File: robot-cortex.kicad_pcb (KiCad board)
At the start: 2 copper layers, 36 parts, among them IC1 ADP2301AUJZ-R7, J1 USB4110GFA, Q1 SS8050-G, Q2 SS8050-G, U1 DF52-4S-0.8H(21), U2 ESP32-WROOM-32E-H4, U3 DF52-5S-0.8H(21), U5 CP2102N-A02-GQFN24R

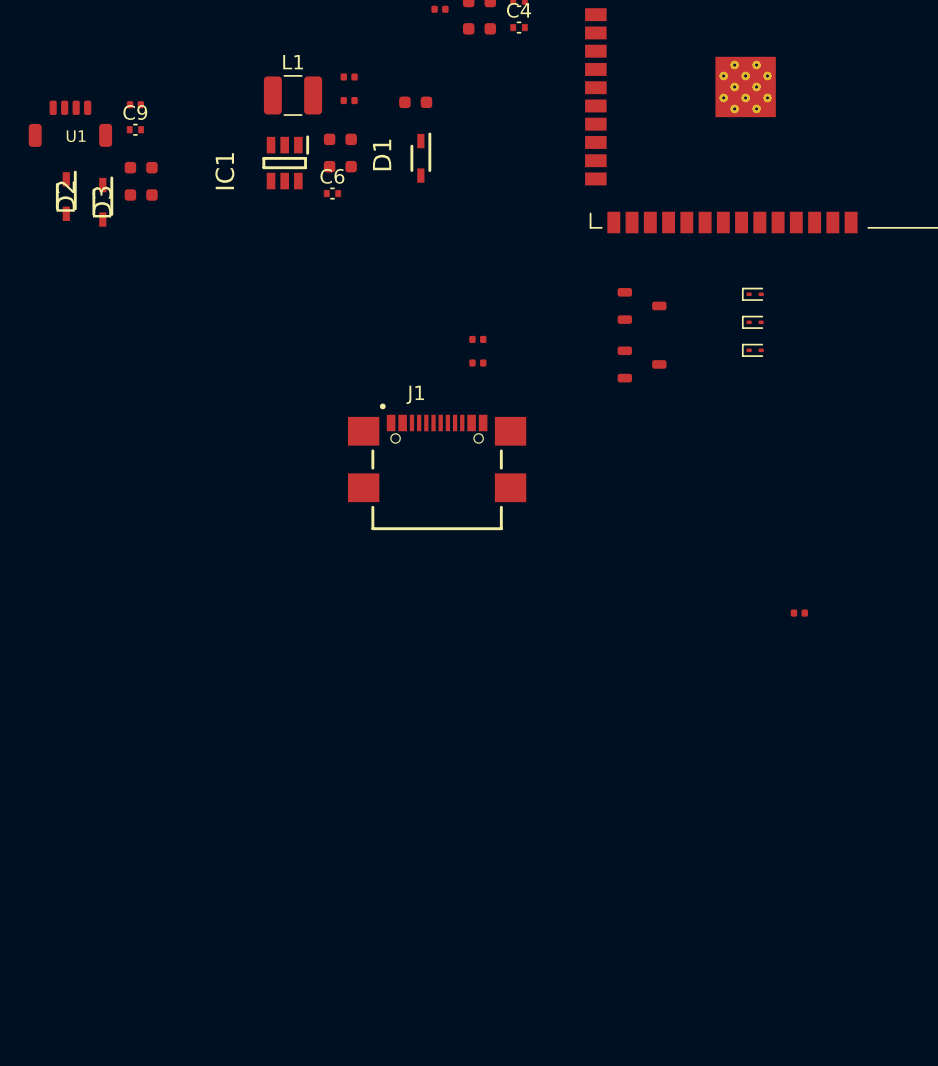
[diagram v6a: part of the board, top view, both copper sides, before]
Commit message: nearly ready to route, need to decide on 5V issue for CAN still
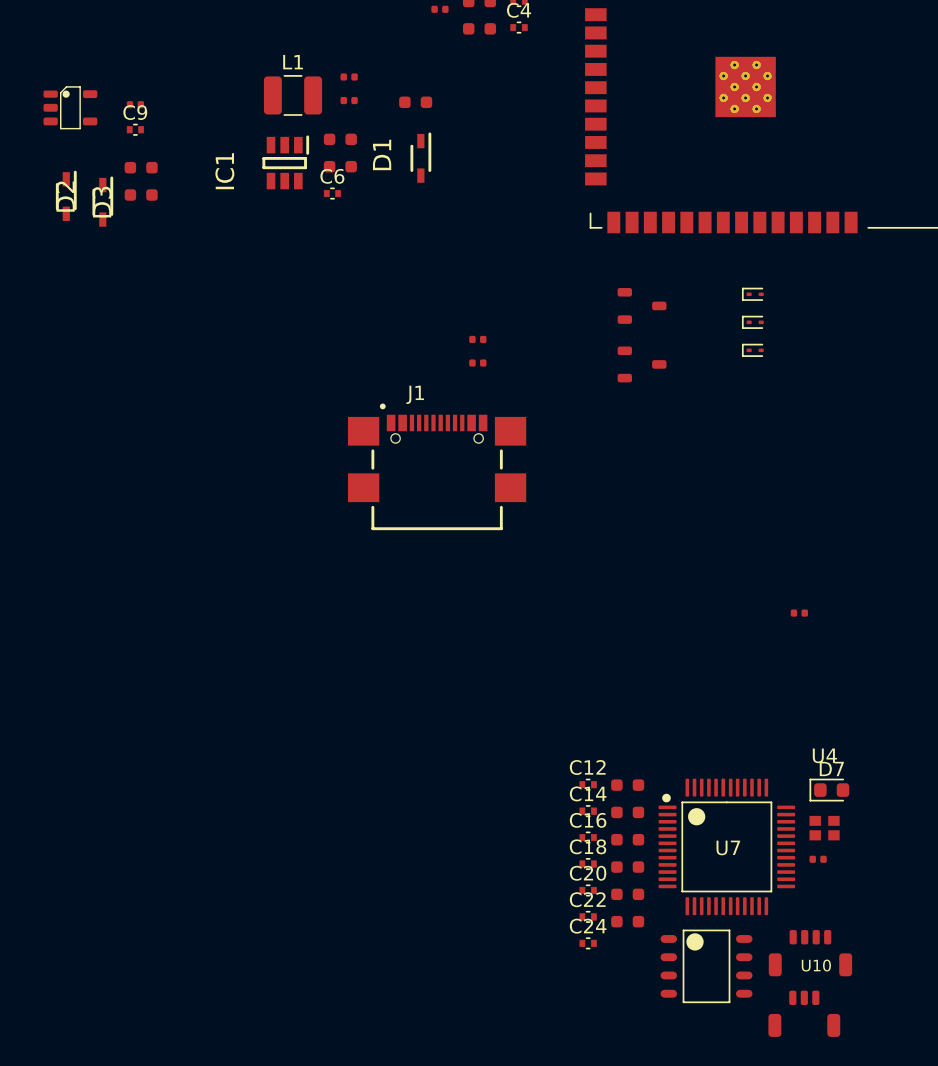
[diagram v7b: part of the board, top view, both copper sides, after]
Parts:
- added C12: 100nF, robot-cortex:C_0402_1005Metric, F.Cu at (85.6, 101.1)
- added C13: C2998534, robot-cortex:C_0603_1608Metric, F.Cu at (88.4, 101.1)
- added C14: 100nF, robot-cortex:C_0402_1005Metric, F.Cu at (85.6, 102.9)
- added C15: C2998534, robot-cortex:C_0603_1608Metric, F.Cu at (88.4, 103.0)
- added C16: 100nF, robot-cortex:C_0402_1005Metric, F.Cu at (85.6, 104.8)
- added C17: C2998534, robot-cortex:C_0603_1608Metric, F.Cu at (88.4, 104.9)
- added C18: 100nF, robot-cortex:C_0402_1005Metric, F.Cu at (85.6, 106.6)
- added C19: C2998534, robot-cortex:C_0603_1608Metric, F.Cu at (88.4, 106.8)
- added C20: 100nF, robot-cortex:C_0402_1005Metric, F.Cu at (85.6, 108.5)
- added C21: C2998534, robot-cortex:C_0603_1608Metric, F.Cu at (88.4, 108.7)
- added C22: 100nF, robot-cortex:C_0402_1005Metric, F.Cu at (85.6, 110.3)
- added C23: C2998534, robot-cortex:C_0603_1608Metric, F.Cu at (88.4, 110.6)
- added C24: 100nF, robot-cortex:C_0402_1005Metric, F.Cu at (85.6, 112.1)
- added D7: C84264, robot-cortex:LED_0603_1608Metric, F.Cu at (102.6, 101.5)
- added R10: 470, robot-cortex:R_0402_1005Metric, F.Cu at (101.6, 106.3)
- added U10: DF52-4S-0.8H(21), robot-cortex:DF52-4S-0.8H(21), F.Cu at (101.1, 111.7)
- added U4: C2901617, robot-cortex:ECS-1633-480-BN-TR, F.Cu at (102.1, 104.1)
- added U7: STM32G431CBT6, robot-cortex:LQFP48-STM32, F.Cu at (95.3, 105.4)
- added U8: TLE9250XSJXUMA1, robot-cortex:SOIC8-TLE5009, F.Cu at (93.9, 113.7)
- added U9: DF52-3S-0.8H(21), robot-cortex:DF52-3S-0.8H(21), F.Cu at (100.7, 115.9)
- U1: value DF52-4S-0.8H(21) -> SPX3819M5-L-5-0; footprint robot-cortex:DF52-4S-0.8H(21) -> robot-cortex:SOT-23-5
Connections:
- net /3V3-Supply/VIN renamed /VDD_MIXED
- net 3v3 renamed +3V3
- U1 pad 2: /VBAT -> GND
- U1 pad 3: GND -> /VBAT
- U1 pad 4: GND -> unconnected-(U1-BYP-Pad4)
- U1 pad 5: GND -> /+5V0
- U2 pad 12: unconnected-(U2-IO27-Pad12) -> /BOOT
- U2 pad 24: unconnected-(U2-IO2-Pad24) -> /NRST
- U2 pad 27: /ESP32/ESP_UART2_RX -> /UART2_TX
- U2 pad 28: /ESP32/ESP_UART2_TX -> /UART2_RX
- U2 pad 29: /ESP32/ESP32_SS -> /SS
- U2 pad 30: /ESP32/ESP32_SCK -> /SPI1_SCK
- U2 pad 31: /ESP32/ESP32_MISO -> /SPI1_MISO
- U2 pad 37: /ESP32/ESP32_MOSI -> /SPI1_MOSI

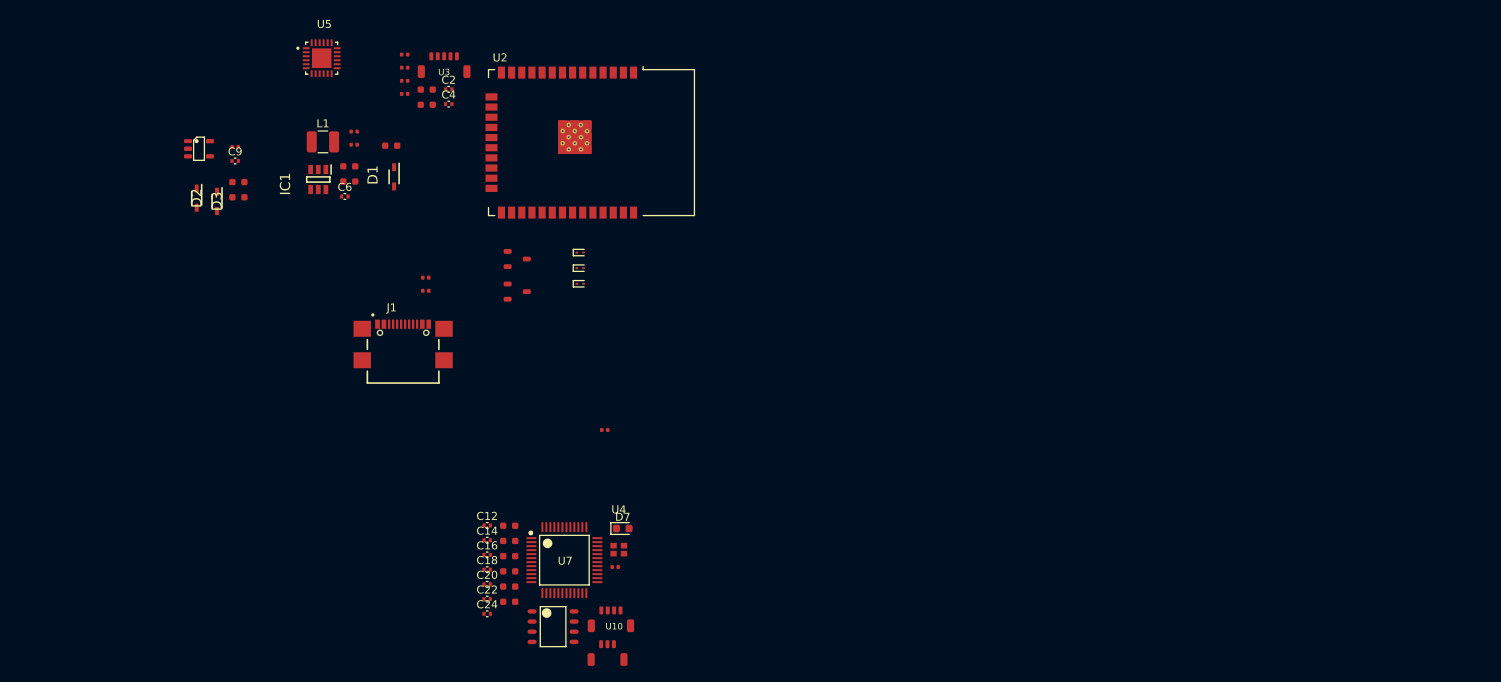
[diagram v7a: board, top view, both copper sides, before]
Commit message: updated power supply method
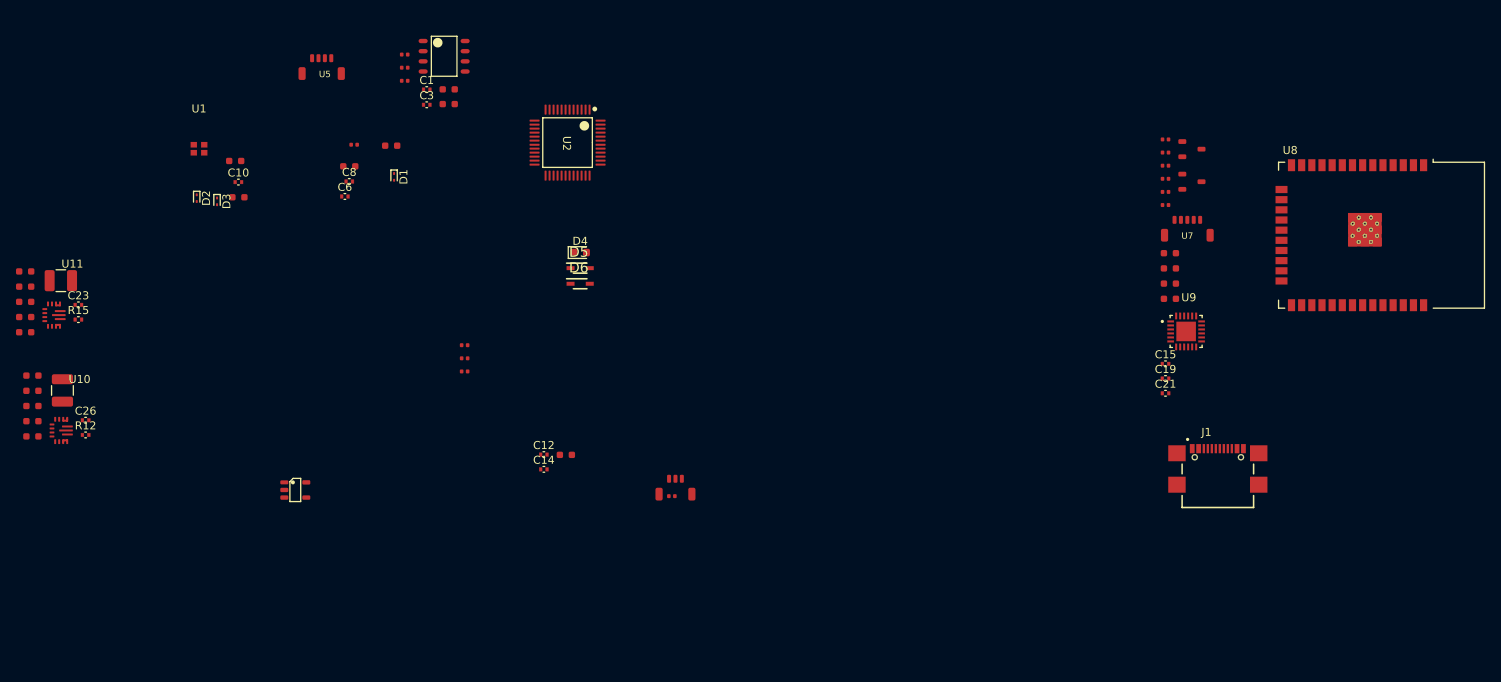
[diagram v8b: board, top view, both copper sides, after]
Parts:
- removed D7: C84264, robot-cortex:LED_0603_1608Metric
- removed IC1: ADP2301AUJZ-R7, robot-cortex:SOT95P280X100-6N
- added C25: C386081, robot-cortex:C_0603_1608Metric, F.Cu at (28.8, 82.3)
- added C26: 100nF, robot-cortex:C_0402_1005Metric, F.Cu at (35.4, 87.9)
- added C27: C2998534, robot-cortex:C_0603_1608Metric, F.Cu at (28.8, 84.2)
- added C28: C2998534, robot-cortex:C_0603_1608Metric, F.Cu at (28.8, 86.2)
- added C29: C2998534, robot-cortex:C_0603_1608Metric, F.Cu at (28.8, 88.0)
- added C30: C2998534, robot-cortex:C_0603_1608Metric, F.Cu at (28.8, 90.0)
- added C31: C2998534, robot-cortex:C_0603_1608Metric, F.Cu at (27.9, 73.1)
- added C32: C2998534, robot-cortex:C_0603_1608Metric, F.Cu at (27.9, 75.0)
- added C33: C2998534, robot-cortex:C_0603_1608Metric, F.Cu at (27.9, 76.9)
- added L2: 1277AS-H-1R0M=P2, robot-cortex:L_1210_3225Metric, F.Cu at (32.5, 84.2)
- added R12: 100k, robot-cortex:C_0402_1005Metric, F.Cu at (35.4, 89.8)
- added R13: 680k, robot-cortex:R_0402_1005Metric, F.Cu at (82.8, 78.5)
- added R14: 130k, robot-cortex:R_0402_1005Metric, F.Cu at (82.8, 80.2)
- added R15: 100k, robot-cortex:C_0402_1005Metric, F.Cu at (34.5, 75.3)
- added R16: 0, robot-cortex:R_0402_1005Metric, F.Cu at (82.8, 81.8)
- added U11: TPS63070, robot-cortex:VQFN-TPS63070, F.Cu at (31.5, 74.8)
- added U6: SPX3819M5-L-5-0, robot-cortex:SOT-23-5, F.Cu at (61.6, 96.6)
- C1, C10, C3, C8: value 4.7uF -> 100nF; footprint robot-cortex:C_0603_1608Metric -> robot-cortex:C_0402_1005Metric
- C11, C5, C7: value 4.7uF -> C2998534
- C15, C19, C21, C23: value C2998534 -> 100nF; footprint robot-cortex:C_0603_1608Metric -> robot-cortex:C_0402_1005Metric
- C16, C18, C20, C4: value 100nF -> 4.7uF; footprint robot-cortex:C_0402_1005Metric -> robot-cortex:C_0603_1608Metric
- C17: value C2998534 -> 4.7uF
- C2, C24, C9: value 100nF -> C2998534; footprint robot-cortex:C_0402_1005Metric -> robot-cortex:C_0603_1608Metric
- C22: value 100nF -> C386081; footprint robot-cortex:C_0402_1005Metric -> robot-cortex:C_0603_1608Metric
- D1, D2, D3: value NSR0530HT1G -> ESD9B3.3ST5G; footprint robot-cortex:SOD2512X110N -> robot-cortex:D_SOD-923
- D4: value ESD9B3.3ST5G -> C84264; footprint robot-cortex:D_SOD-923 -> robot-cortex:LED_0603_1608Metric
- D5, D6: value ESD9B3.3ST5G -> NSR0530HT1G; footprint robot-cortex:D_SOD-923 -> robot-cortex:SOD2512X110N
- L1: value 2.2uH -> 1277AS-H-1R0M=P2; footprint Inductor_SMD:L_1210_3225Metric -> robot-cortex:L_1210_3225Metric
- R1, R2: value 10k -> 5.1k
- R10: value 470 -> 470k
- R11: value 10.2k -> 150k
- R3: value 1k -> 470
- R4: value 22k -> 10k
- R5: value 31.6k -> 10k
- R7: value 5.1k -> 22k
- R8: value 5.1k -> 47.5k
- R9: value 47.5k -> 1k
- U1: value SPX3819M5-L-5-0 -> C2901617; footprint robot-cortex:SOT-23-5 -> robot-cortex:ECS-1633-480-BN-TR
- U10: value DF52-4S-0.8H(21) -> TPS63070; footprint robot-cortex:DF52-4S-0.8H(21) -> robot-cortex:VQFN-TPS63070
- U2: value ESP32-WROOM-32E-H4 -> STM32G431CBT6; footprint robot-cortex:ESP32-WROOM-32 -> robot-cortex:LQFP48-STM32
- U3: value DF52-5S-0.8H(21) -> TLE9250XSJXUMA1; footprint robot-cortex:DF52-5S-0.8H(21) -> robot-cortex:SOIC8-TLE5009
- U4: value C2901617 -> DF52-3S-0.8H(21); footprint robot-cortex:ECS-1633-480-BN-TR -> robot-cortex:DF52-3S-0.8H(21)
- U5: value CP2102N-A02-GQFN24R -> DF52-4S-0.8H(21); footprint robot-cortex:QFN50P400X400X80-25N -> robot-cortex:DF52-4S-0.8H(21)
- U7: value STM32G431CBT6 -> DF52-5S-0.8H(21); footprint robot-cortex:LQFP48-STM32 -> robot-cortex:DF52-5S-0.8H(21)
- U8: value TLE9250XSJXUMA1 -> ESP32-WROOM-32E-H4; footprint robot-cortex:SOIC8-TLE5009 -> robot-cortex:ESP32-WROOM-32
- U9: value DF52-3S-0.8H(21) -> CP2102N-A02-GQFN24R; footprint robot-cortex:DF52-3S-0.8H(21) -> robot-cortex:QFN50P400X400X80-25N
- moved R6 116.3 mm to (170.4, 56.1)
- moved U8 111.8 mm to (194.4, 64.8), turned to -90 degrees
- moved J1 103.0 mm to (176.9, 92.6)
- moved R5 101.5 mm to (170.4, 54.5)
- moved R4 95.3 mm to (170.4, 52.8)
- moved C16 93.3 mm to (171.0, 67.0)
- moved R7 93.3 mm to (170.4, 57.8)
- moved R8 93.3 mm to (170.4, 59.4)
- moved C18 92.5 mm to (171.0, 70.8)
- moved C20 92.5 mm to (171.0, 72.8)
- moved C17 90.1 mm to (171.0, 69.0)
- moved U7 88.7 mm to (173.1, 62.9)
- moved C21 85.5 mm to (170.4, 84.6)
- moved C19 85.5 mm to (170.4, 82.7)
- moved Q1 85.5 mm to (173.7, 54.0)
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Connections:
- C1 pad 1: +3V3 -> /NRST
- C11 pad 1: +3V3 -> /VBAT
- C12 pad 1: /NRST -> /VBAT
- C13 pad 1: +3V3 -> /+5V0
- C14 pad 1: +3V3 -> /+5V0
- C15 pad 1: +3V3 -> /ESP32/EN
- C21 pad 1: /VBAT -> +3V3
- C22 pad 1: /VBAT -> /VDD_MIXED
- C23 pad 1: /+5V0 -> Net-(U11-VAUX)
- C4 pad 1: +3V3 -> /VUSB
- C5 pad 1: /VUSB -> +3V3
- C6 pad 1: Net-(IC1-BST) -> +3V3
- C6 pad 2: Net-(D1-K) -> GND
- C9 pad 1: /ESP32/EN -> +3V3
- D1 pad 1: Net-(D1-K) -> GND
- D1 pad 2: GND -> /D-
- D2 pad 1: /VDD_MIXED -> GND
- D2 pad 2: /VBAT -> /D+
- D3 pad 1: /VDD_MIXED -> GND
- D4 pad 1: GND -> Net-(D4-K)
- D4 pad 2: /VUSB -> /LED
- D5 pad 1: GND -> /VDD_MIXED
- D5 pad 2: /D+ -> /VBAT
- D6 pad 1: GND -> /VDD_MIXED
- D6 pad 2: /D- -> /VUSB
- L1 pad 1: Net-(D1-K) -> Net-(U11-L1)
- L1 pad 2: +3V3 -> Net-(U11-L2)
- R1 pad 1: /ESP32/RTS -> GND
- R1 pad 2: Net-(Q2-B) -> Net-(J1-CC1)
- R10 pad 1: Net-(D7-K) -> +3V3
- R10 pad 2: GND -> /PSU_TPS63070RNMR/FB
- R11 pad 1: GND -> /PSU_TPS63070RNMR/FB
- R11 pad 2: /3V3-Supply/FB -> GND
- R2 pad 1: /ESP32/DTR -> GND
- R2 pad 2: Net-(Q1-B) -> Net-(J1-CC2)
- R3 pad 1: Net-(U5-~{RST}) -> Net-(D4-K)
- R3 pad 2: +3V3 -> GND
- R4 pad 1: /ESP32/CP210x_VBUS -> /ESP32/EN
- R4 pad 2: /VUSB -> +3V3
- R5 pad 1: /3V3-Supply/FB -> /ESP32/RTS
- R5 pad 2: +3V3 -> Net-(Q2-B)
- R6 pad 1: /ESP32/EN -> /ESP32/DTR
- R6 pad 2: +3V3 -> Net-(Q1-B)
- R7 pad 1: GND -> /ESP32/CP210x_VBUS
- R7 pad 2: Net-(J1-CC1) -> /VUSB
- R8 pad 2: Net-(J1-CC2) -> /ESP32/CP210x_VBUS
- R9 pad 1: GND -> Net-(U9-~{RST})
- R9 pad 2: /ESP32/CP210x_VBUS -> +3V3
- U1 pad 1: /VBAT -> +3V3
- U1 pad 3: /VBAT -> Net-(U1-OUTPUT)
- U1 pad 4: unconnected-(U1-BYP-Pad4) -> +3V3
- U10 pad 1: /VBAT -> /VDD_MIXED
- U10 pad 2: /CANL -> Net-(U10-PG)
- U10 pad 3: /CANH -> Net-(U10-VAUX)
- U10 pad 5: GND -> /PSU_TPS63070RNMR/FB
- U2 pad 1: GND -> +3V3
- U2 pad 10: unconnected-(U2-IO25-Pad10) -> /UART2_TX
- U2 pad 11: unconnected-(U2-IO26-Pad11) -> /UART2_RX
- U2 pad 12: /BOOT -> unconnected-(U2-PA4-Pad12)
- U2 pad 13: /ESP32/TMS -> unconnected-(U2-PA5-Pad13)
- U2 pad 14: /ESP32/TDI -> unconnected-(U2-PA6-Pad14)
- U2 pad 15: GND -> unconnected-(U2-PA7-Pad15)
- U2 pad 16: /ESP32/TCK -> /ISENSE_A
- U2 pad 17: unconnected-(U2-NC-Pad17) -> /ISENSE_B
- U2 pad 19: unconnected-(U2-NC-Pad19) -> GND
- U2 pad 2: +3V3 -> unconnected-(U2-PC13-Pad2)
- U2 pad 20: unconnected-(U2-NC-Pad20) -> +3V3
- U2 pad 21: unconnected-(U2-NC-Pad21) -> +3V3
- U2 pad 22: unconnected-(U2-NC-Pad22) -> /LED
- U2 pad 23: /ESP32/TDO -> GND
- U2 pad 24: /NRST -> +3V3
- U2 pad 25: /ESP32/IO0 -> /ISENSE_C
- U2 pad 26: unconnected-(U2-IO4-Pad26) -> /ENABLE
- U2 pad 27: /UART2_TX -> unconnected-(U2-PB13-Pad27)
- U2 pad 28: /UART2_RX -> unconnected-(U2-PB14-Pad28)
- U2 pad 29: /SS -> unconnected-(U2-PB15-Pad29)
- U2 pad 3: /ESP32/EN -> unconnected-(U2-PC14-Pad3)
- U2 pad 30: /SPI1_SCK -> unconnected-(U2-PA8-Pad30)
- U2 pad 31: /SPI1_MISO -> unconnected-(U2-PA9-Pad31)
- U2 pad 33: unconnected-(U2-IO21-Pad33) -> /FDCAN1_RX
- U2 pad 34: /ESP32/CP210x_TX -> /FDCAN1_TX
- U2 pad 35: /ESP32/CP210x_RX -> GND
- U2 pad 36: unconnected-(U2-IO22-Pad36) -> +3V3
- U2 pad 37: /SPI1_MOSI -> /SWDIO
- U2 pad 38: GND -> /SWCLK
- U2 pad 39: GND -> unconnected-(U2-PA15-Pad39)
- U2 pad 5: unconnected-(U2-SENSOR_VN-Pad5) -> Net-(U1-OUTPUT)
- U2 pad 7: unconnected-(U2-IO35-Pad7) -> /NRST
- U2 pad 8: unconnected-(U2-IO32-Pad8) -> /COS
- U2 pad 9: unconnected-(U2-IO33-Pad9) -> /SIN
- U3 pad 1: /ESP32/TDO -> /FDCAN1_TX
- U3 pad 2: /ESP32/TMS -> GND
- U3 pad 3: /ESP32/TDI -> /+5V0
- U3 pad 4: /ESP32/TCK -> /FDCAN1_RX
- U3 pad 5: GND -> +3V3
- U3 pad 6: GND -> /CANL
- U3 pad 7: GND -> /CANH
- U4 pad 1: +3V3 -> /SWDIO
- U4 pad 2: GND -> /SWCLK
- U4 pad 3: Net-(U4-OUTPUT) -> GND
- U4 pad 4: +3V3 -> GND
- U5 pad 1: unconnected-(U5-~{RI}/CLK-Pad1) -> /VBAT
- U5 pad 2: GND -> /CANL
- U5 pad 3: /D+ -> /CANH
- U5 pad 4: /D- -> GND
- U5 pad 5: +3V3 -> GND
- U5 pad 6: +3V3 -> GND
- U7 pad 1: +3V3 -> /ESP32/TDO
- U7 pad 2: unconnected-(U7-PC13-Pad2) -> /ESP32/TMS
- U7 pad 3: unconnected-(U7-PC14-Pad3) -> /ESP32/TDI
- U7 pad 4: unconnected-(U7-PC15-Pad4) -> /ESP32/TCK
- U7 pad 5: Net-(U4-OUTPUT) -> GND
- U7 pad 6: unconnected-(U7-PF1-OSC_OUT-Pad6) -> GND
- U7 pad 7: /NRST -> GND
- U8 pad 1: /FDCAN1_TX -> GND
- U8 pad 2: GND -> +3V3
- U8 pad 3: /+5V0 -> /ESP32/EN
- U8 pad 4: /FDCAN1_RX -> unconnected-(U8-SENSOR_VP-Pad4)
- U8 pad 5: +3V3 -> unconnected-(U8-SENSOR_VN-Pad5)
- U8 pad 6: /CANL -> unconnected-(U8-IO34-Pad6)
- U8 pad 7: /CANH -> unconnected-(U8-IO35-Pad7)
- U8 pad 8: GND -> unconnected-(U8-IO32-Pad8)
- U9 pad 1: /SWDIO -> unconnected-(U9-~{RI}/CLK-Pad1)
- U9 pad 2: /SWCLK -> GND
- U9 pad 3: GND -> /D+
- U9 pad 4: GND -> /D-
- U9 pad 5: GND -> +3V3
